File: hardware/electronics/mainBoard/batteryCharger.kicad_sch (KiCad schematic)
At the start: 49 parts, among them J18 M8AS-02PFFR-SF8001, J19 S2B-PH-SM4-TB, Q1 CSD17581Q3A, Q2 CSD17581Q3A, Q3 CSD17581Q3A, Q4 CSD17581Q3A, Q5 CSD17575Q3, U22 BQ25798

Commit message: cleaned
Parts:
- removed C115: 2.2uF, symbol lib_sch:C
- removed C125: 47nF, symbol lib_sch:C
- removed C126: 4.7uF, symbol lib_sch:C
- removed F1: 2920L500/24SLDR, symbol lib_sch:F_horizontal
- removed NT8, NT9: NetTie_2, symbol lib_sch:NetTie_2
- removed R67: 2R2, symbol lib_sch:R
- added C137: 47nF, symbol lib_sch:C_horizontal
- added C138: 4.7uF, symbol lib_sch:C_horizontal
- added J23: MUSBRM1C1M0, symbol lib_sch:USB_C_Receptacle_24P
- added NT10, NT9: NetTie, symbol lib_sch:NetTie
- added R83, R84: 5K1, symbol lib_sch:R
- D21: renamed from D16; Color GREEN -> (none)
- Q9: renamed from Q5; value CSD17575Q3 -> CSD17581Q3A; DKPN 296-35628-1-ND -> 296-47754-1-ND; ID 100A -> 21A; MPN CSD18532Q5B -> CSD17581Q3A; RDSON 3.2mR -> 3m8R; VDSS 60V -> 30V; VGSTH 2V2 -> 1V7
- U24: renamed from U22; DKPN (none) -> 296-BQ25798RQMRCT-ND; MPN BQ25798 -> BQ25798RQMR
- renumbered C106 to C118, C107 to C119, C108 to C120, C109 to C121, C110 to C122, C111 to C123, C112 to C124, C113 to C125, C114 to C126, C116 to C127, C117 to C128, C118 to C129, C119 to C130, C120 to C131, C121 to C132, C122 to C133, C123 to C134, C124 to C135, C127 to C136, D14 to D19, D15 to D20, J18 to J22, J19 to J24, JP10 to JP12, L6 to L8, Q1 to Q5, Q2 to Q6, Q3 to Q7, Q4 to Q8, R66 to R80, R68 to R81, R69 to R82, R70 to R85, R71 to R86, R72 to R87, R73 to R88, R74 to R89, R75 to R90, R76 to R91
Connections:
- net AGND: now also NT9.2
- net BATP: now also C137.1
- net GND: now also U24.27 (GND), C137.2, C138.2, J23.A1 (GND), J23.A12 (GND), J23.B1 (GND), J23.B12 (GND), J23.S1, J23.S2, NT10.1, NT9.1, R83.2, R84.2
- net REGN: now also JP12.1, C138.1; no longer R86.1
- net VAC2: now also J22.1 (VDD)
- net VSS: now also NT10.2; no longer U24.27 (GND)
- net at D21.2: now also U24.1 (STAT); no longer JP12.1
- net at JP12.2: now also R86.1; no longer U24.1 (STAT)
- net BTST1: now reaches C133.1, U24.4 (BTST1)
- net PPHV renamed VBUS
- net VBUS: now also J23.A4 (VBUS), J23.A9 (VBUS), J23.B4 (VBUS), J23.B9 (VBUS)
- new net CC1: J23.A5 (CC1), R83.1
- new net CC2: J23.B5 (CC2), R84.1
- new net USB_FS.DN: J23.A7 (D1-), J23.B7 (D2-)
- new net USB_FS.DP: J23.A6 (D1+), J23.B6 (D2+)
- no-connect marks 4 -> 14
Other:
- note added: "Upstream Facing USB Port"
- note added: "VIN: 5V@3A"
- note removed: "USB PD"
- note removed: "VIN: 5-20V"
- moved on the sheet: C118, C126, C134, C135, D19, D20, D21, J22, JP12, L8, Q5, Q6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

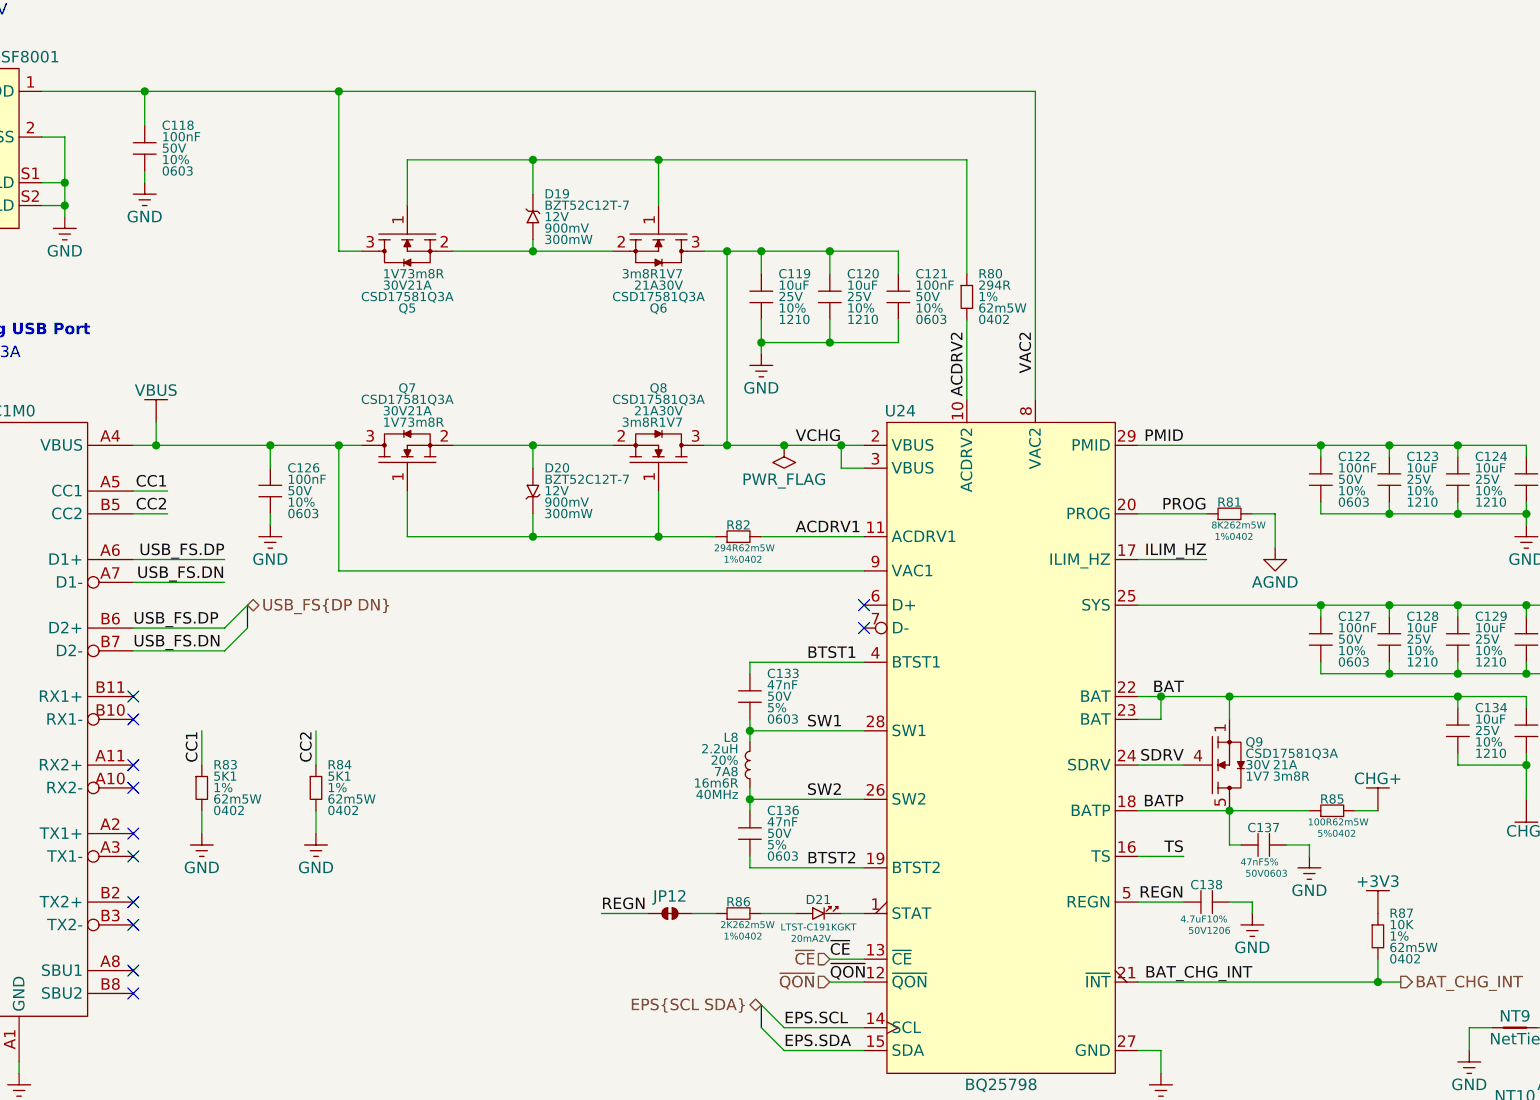
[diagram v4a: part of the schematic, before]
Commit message: updated capacitors
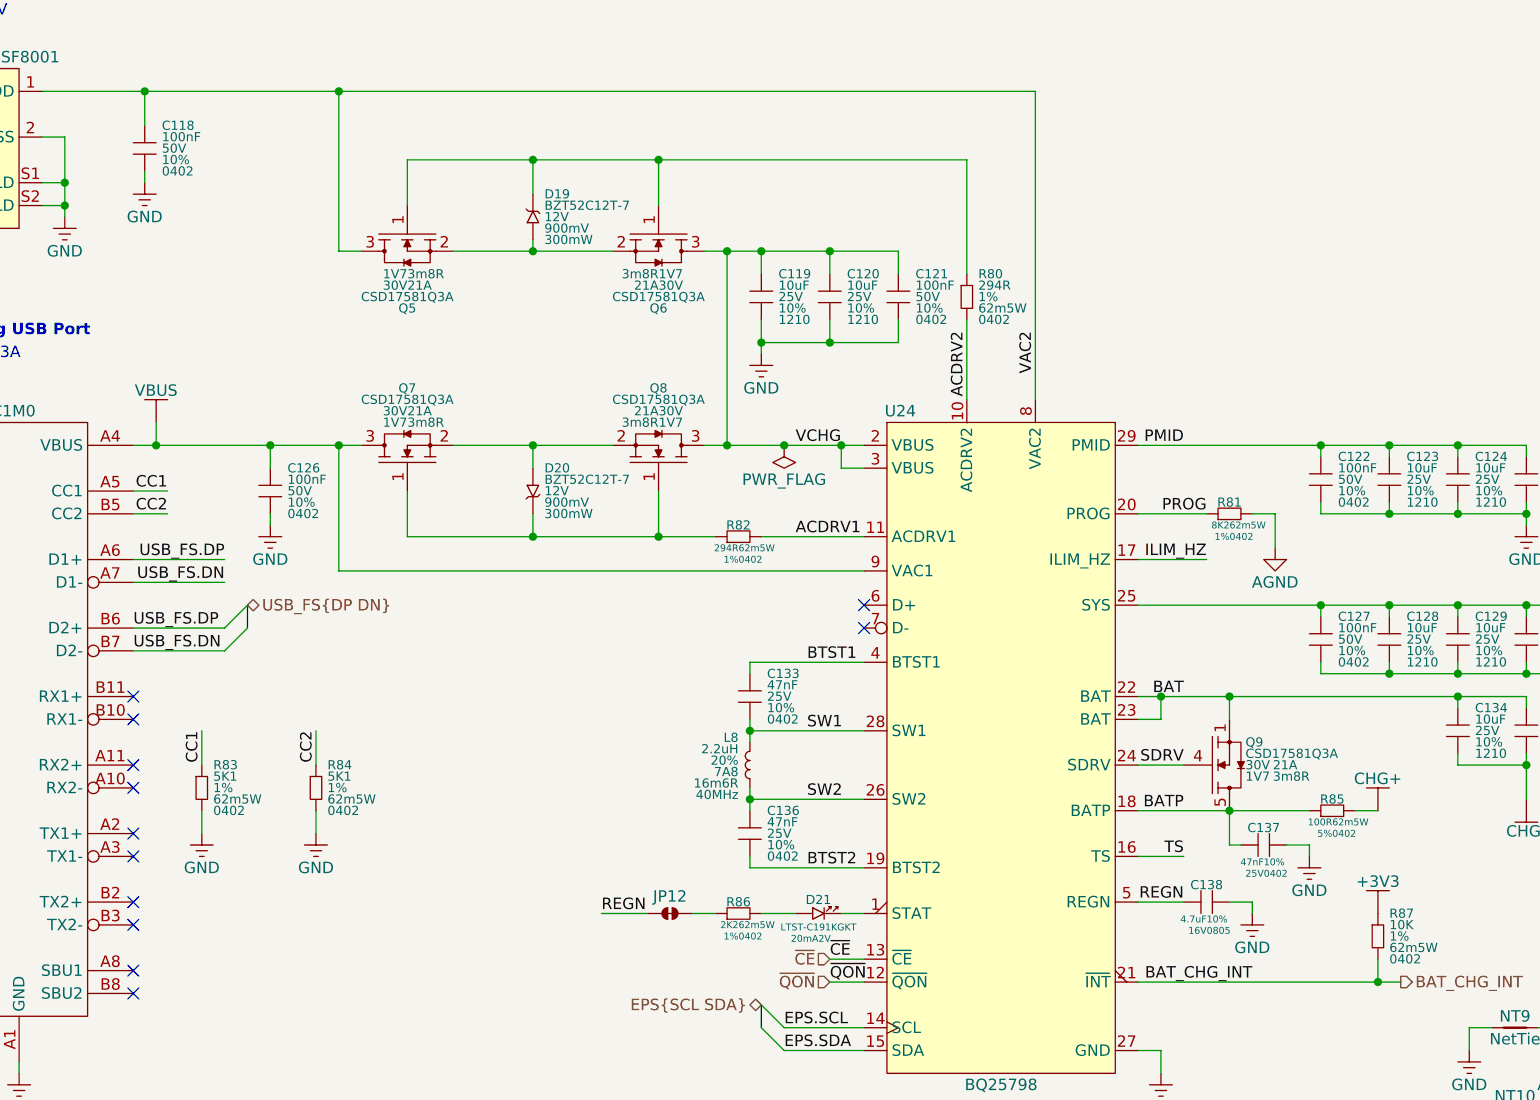
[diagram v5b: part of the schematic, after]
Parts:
- C118, C121, C122, C126, C127: DKPN 478-KAM15AR71H104KTCT-ND -> 490-GRT155R71H104KE01DCT-ND; MPN 06035C104K4T2A -> GRT155R71H104KE01D; Manufacturer KYOCERA AVX -> Murata Electronics; Package 0603 -> 0402
- C133, C136, C137: DKPN 478-KAM15AR71H472JTCT-ND -> 490-GRT155R71E473KE01DCT-ND; MPN 06035C472J4T2A -> GRT155R71E473KE01D; Manufacturer KYOCERA AVX -> Murata Electronics; Package 0603 -> 0402; Tolerance 5% -> 10%; Voltage Rating 50V -> 25V
- C138: DKPN 478-KAM31GR71H475KLCT-ND -> 490-GRT21BR71C475KE13LCT-ND; MPN 12065C475K4T4A -> GRT21BR71C475KE13L; Manufacturer KYOCERA AVX -> Murata Electronics; Package 1206 -> 0805; Voltage Rating 50V -> 16V

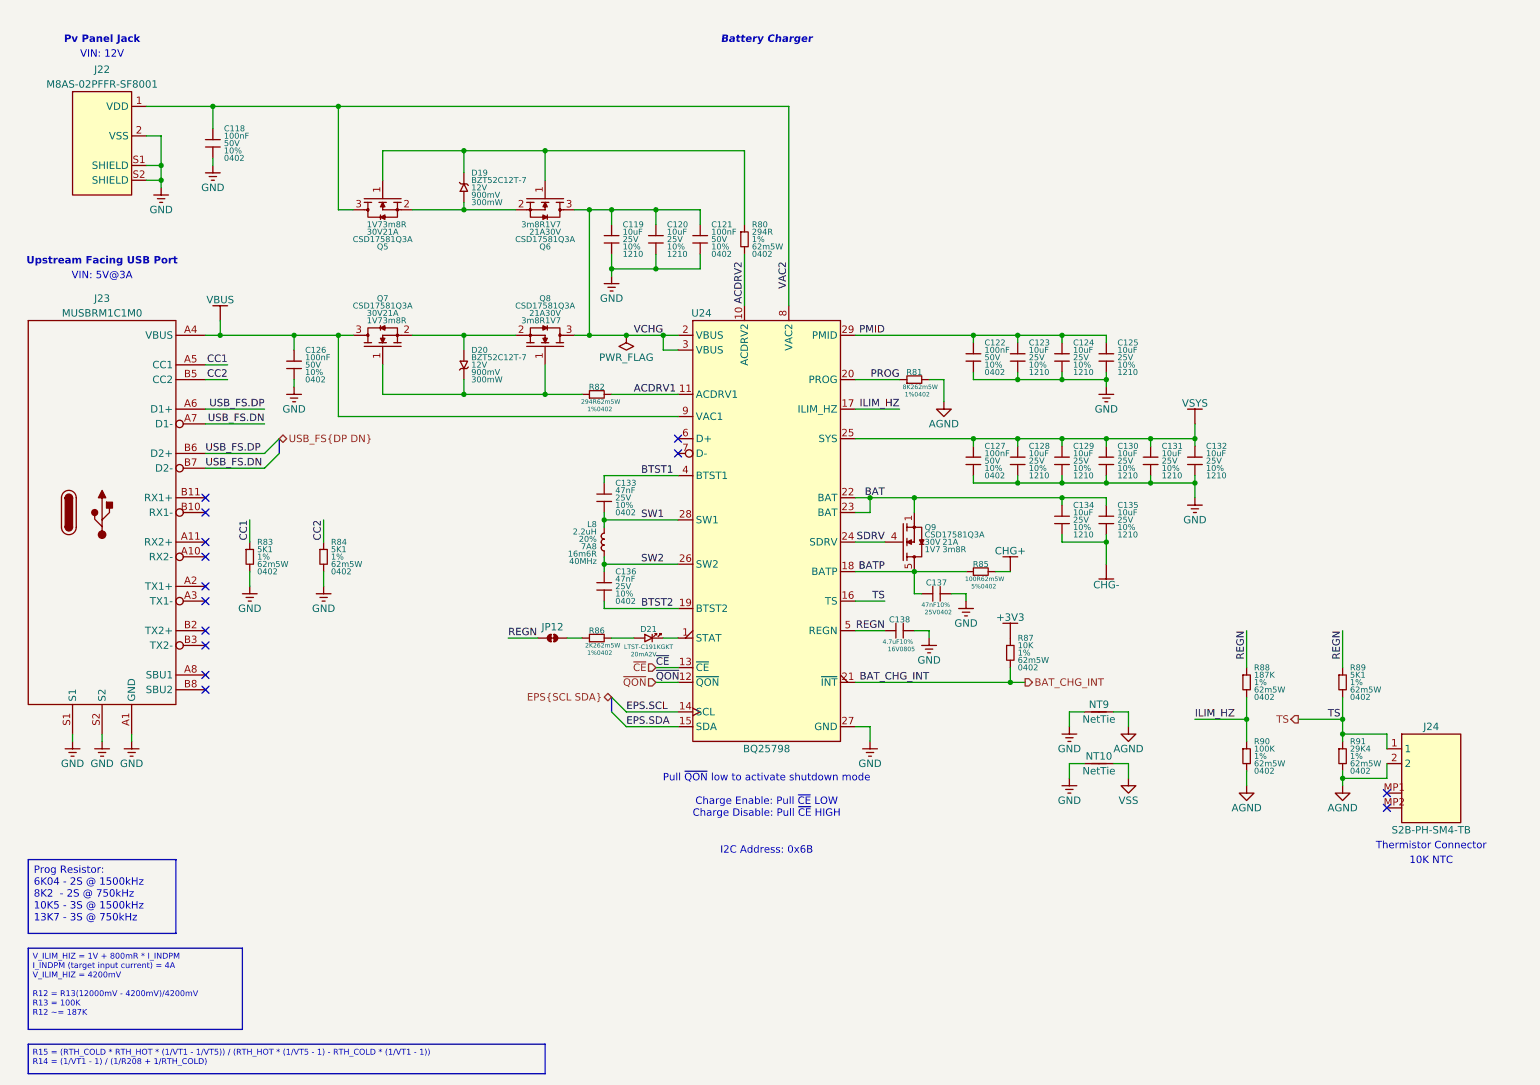
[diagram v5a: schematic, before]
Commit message: added testpoints and fixed AGND
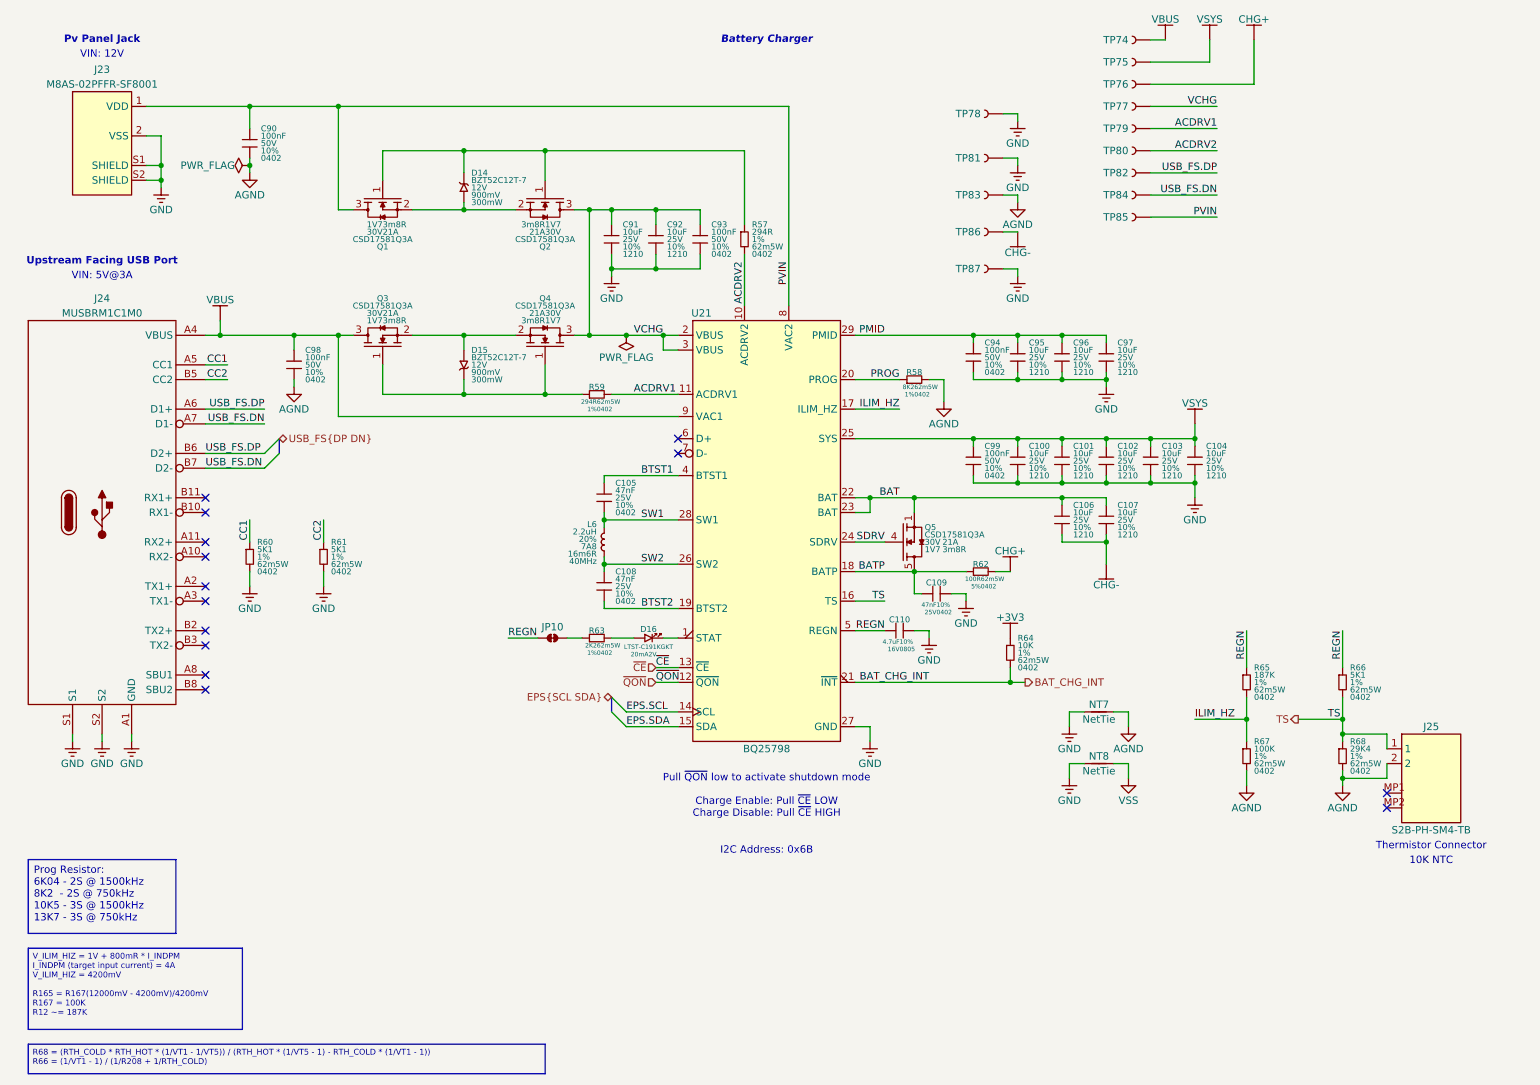
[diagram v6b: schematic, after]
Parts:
- added TP74, TP75, TP76, TP77, TP79, TP80, TP82, TP84, TP85: ~, symbol lib_sch:Testpoint
- added TP78, TP81, TP83, TP86, TP87: RCWCTE, symbol lib_sch:Testpoint
- renumbered C128 to C100, C129 to C101, C130 to C102, C131 to C103, C132 to C104, C133 to C105, C134 to C106, C135 to C107, C136 to C108, C137 to C109, C138 to C110, C118 to C90, C119 to C91, C120 to C92, C121 to C93, C122 to C94, C123 to C95, C124 to C96, C125 to C97, C126 to C98, C127 to C99, D19 to D14, D20 to D15, D21 to D16, J22 to J23, J23 to J24, J24 to J25, JP12 to JP10, L8 to L6, NT9 to NT7, NT10 to NT8, Q5 to Q1, Q6 to Q2, Q7 to Q3, Q8 to Q4, Q9 to Q5, R80 to R57, R81 to R58, R82 to R59, R83 to R60, R84 to R61, R85 to R62, R86 to R63, R87 to R64, R88 to R65, R89 to R66, R90 to R67, R91 to R68, U24 to U21
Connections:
- net ACDRV1: now also TP79.1
- net ACDRV2: now also TP80.1
- net AGND: now also C90.2, C98.2, TP83.1
- net CHG+: now also TP76.1
- net CHG-: now also TP86.1
- net GND: now also TP78.1, TP81.1, TP87.1; no longer C90.2, C98.2
- net USB_FS.DN: now also TP84.1
- net USB_FS.DP: now also TP82.1
- net VBUS: now also TP74.1
- net VCHG: now also TP77.1
- net VSYS: now also TP75.1
- net VAC2 renamed PVIN
- net PVIN: now also TP85.1
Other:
- moved on the sheet: C90

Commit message: updated symbol refs
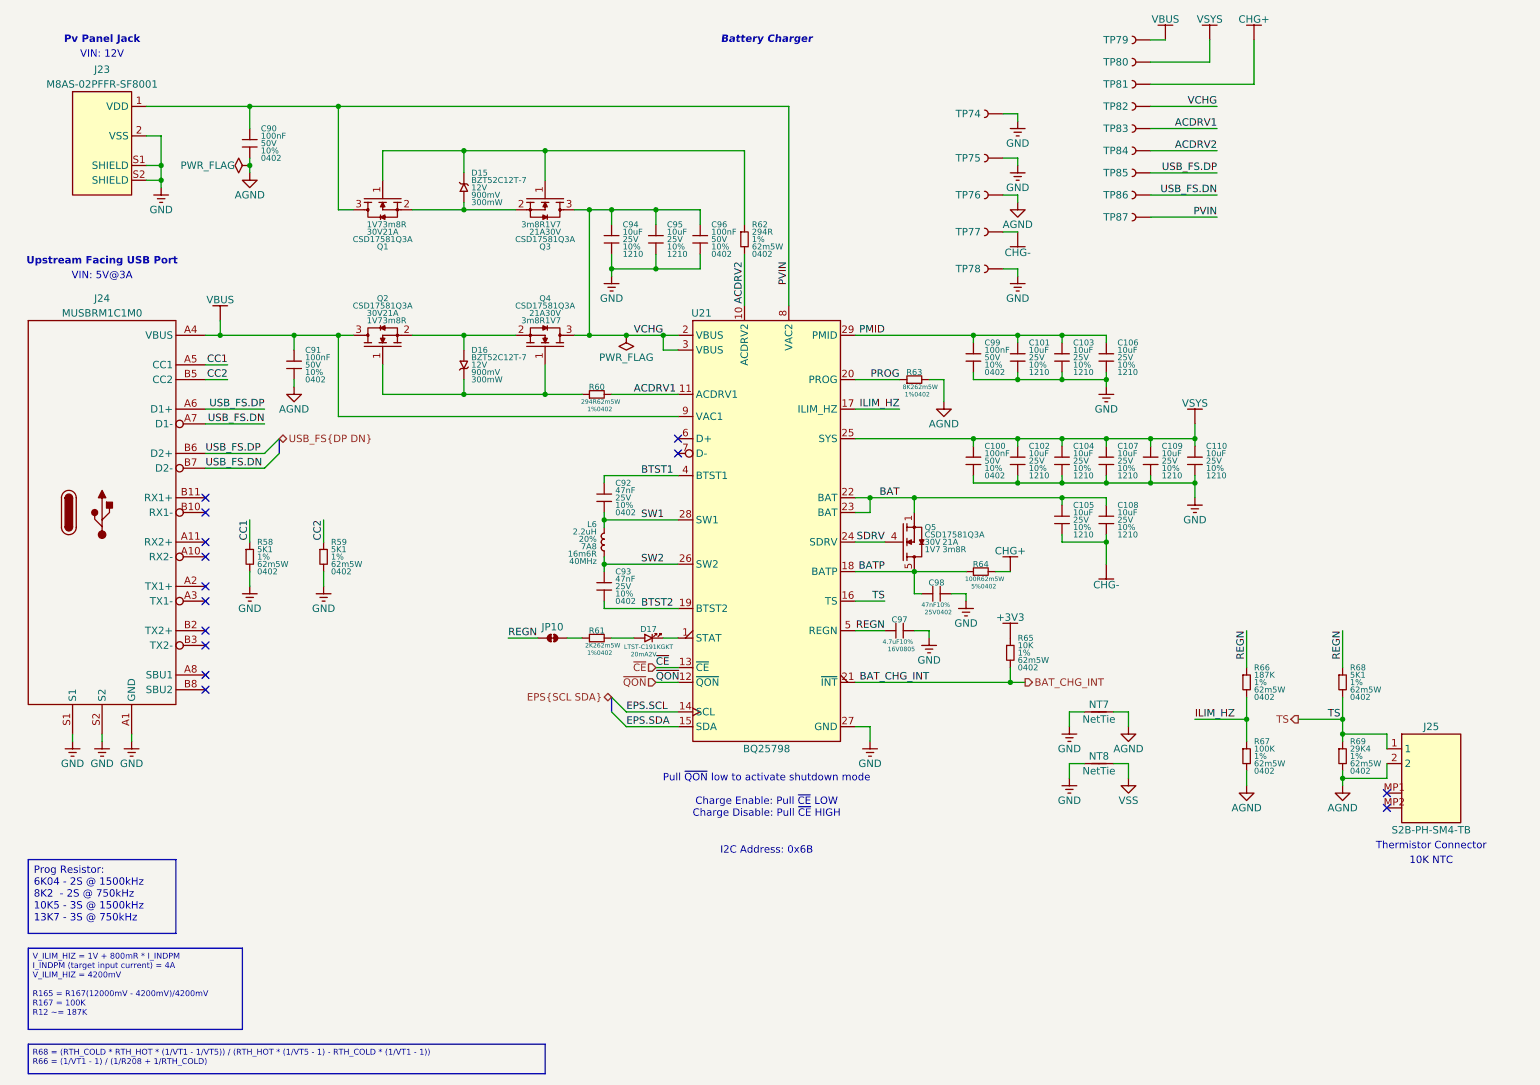
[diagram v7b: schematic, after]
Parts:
- renumbered C99 to C100, C95 to C101, C100 to C102, C96 to C103, C101 to C104, C106 to C105, C97 to C106, C102 to C107, C107 to C108, C103 to C109, C104 to C110, C98 to C91, C105 to C92, C108 to C93, C91 to C94, C92 to C95, C93 to C96, C110 to C97, C109 to C98, C94 to C99, D14 to D15, D15 to D16, D16 to D17, Q3 to Q2, Q2 to Q3, R60 to R58, R61 to R59, R59 to R60, R63 to R61, R57 to R62, R58 to R63, R62 to R64, R64 to R65, R65 to R66, R66 to R68, R68 to R69, TP78 to TP74, TP81 to TP75, TP83 to TP76, TP86 to TP77, TP87 to TP78, TP74 to TP79, TP75 to TP80, TP76 to TP81, TP77 to TP82, TP79 to TP83, TP80 to TP84, TP82 to TP85, TP84 to TP86, TP85 to TP87
